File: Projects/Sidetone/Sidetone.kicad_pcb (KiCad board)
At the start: 2 copper layers, 100 x 100 mm, 48 parts, among them Q1 2N3904, Q2 2N3904, Q3 2N3904, U1 4N35, U2 LM324, U3 LM386

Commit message: 20240216
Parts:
- moved C3 77.4 mm to (191.0, 94.5)
- moved R19 42.2 mm to (214.1, 44.2)
- moved R24 39.6 mm to (211.8, 63.0)
- moved C2 34.4 mm to (90.9, 56.4)
- moved C1 30.9 mm to (93.0, 36.9)
- moved R20 30.1 mm to (203.2, 36.6)
- moved R23 25.0 mm to (197.6, 55.4)
- moved R22 23.9 mm to (186.7, 66.0)
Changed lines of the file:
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@@
   (net 35 "unconnected-(U3-GAIN-Pad1)")
   (footprint "Capacitor_THT:CP_Radial_D8.0mm_P3.80mm" (layer "F.Cu")
-    (at 123.885058 46.443284)
+    (at 90.932 56.388)
     (descr "CP, Radial series, Radial, pin pitch=3.80mm, , diameter=8mm, Electrolytic Capacitor")
     (tags "CP Radial series Radial pin pitch 3.80mm  diameter 8mm Electrolytic Capacitor")
@@
   )
   (footprint "Resistor_THT:R_Axial_DIN0207_L6.3mm_D2.5mm_P7.62mm_Horizontal" (layer "F.Cu")
-    (at 173.16036 46.293284)
+    (at 186.69 66.04)
     (descr "Resistor, Axial_DIN0207 series, Axial, Horizontal, pin pitch=7.62mm, 0.25W = 1/4W, length*diameter=6.3*2.5mm^2, http://cdn-reichelt.de/documents/datenblatt/B400/1_4W%23YAG.pdf")
     (tags "Resistor Axial_DIN0207 series Axial Horizontal pin pitch 7.62mm 0.25W = 1/4W length 6.3mm diameter 2.5mm")
@@
   )
   (footprint "Capacitor_THT:CP_Radial_D8.0mm_P3.80mm" (layer "F.Cu")
-    (at 123.885058 36.893284)
+    (at 92.964 36.893284)
     (descr "CP, Radial series, Radial, pin pitch=3.80mm, , diameter=8mm, Electrolytic Capacitor")
     (tags "CP Radial series Radial pin pitch 3.80mm  diameter 8mm Electrolytic Capacitor")
@@
   )
   (footprint "Resistor_THT:R_Axial_DIN0207_L6.3mm_D2.5mm_P7.62mm_Horizontal" (layer "F.Cu")
-    (at 173.16036 54.393284)
+    (at 211.836 62.992)
     (descr "Resistor, Axial_DIN0207 series, Axial, Horizontal, pin pitch=7.62mm, 0.25W = 1/4W, length*diameter=6.3*2.5mm^2, http://cdn-reichelt.de/documents/datenblatt/B400/1_4W%23YAG.pdf")
     (tags "Resistor Axial_DIN0207 series Axial Horizontal pin pitch 7.62mm 0.25W = 1/4W length 6.3mm diameter 2.5mm")
@@
   )
   (footprint "Resistor_THT:R_Axial_DIN0207_L6.3mm_D2.5mm_P7.62mm_Horizontal" (layer "F.Cu")
-    (at 173.16036 34.143284)
+    (at 214.122 44.196)
     (descr "Resistor, Axial_DIN0207 series, Axial, Horizontal, pin pitch=7.62mm, 0.25W = 1/4W, length*diameter=6.3*2.5mm^2, http://cdn-reichelt.de/documents/datenblatt/B400/1_4W%23YAG.pdf")
     (tags "Resistor Axial_DIN0207 series Axial Horizontal pin pitch 7.62mm 0.25W = 1/4W length 6.3mm diameter 2.5mm")
@@
   )
   (footprint "Resistor_THT:R_Axial_DIN0207_L6.3mm_D2.5mm_P7.62mm_Horizontal" (layer "F.Cu")
-    (at 173.16036 38.193284)
+    (at 203.2 36.576)
     (descr "Resistor, Axial_DIN0207 series, Axial, Horizontal, pin pitch=7.62mm, 0.25W = 1/4W, length*diameter=6.3*2.5mm^2, http://cdn-reichelt.de/documents/datenblatt/B400/1_4W%23YAG.pdf")
     (tags "Resistor Axial_DIN0207 series Axial Horizontal pin pitch 7.62mm 0.25W = 1/4W length 6.3mm diameter 2.5mm")
@@
   )
   (footprint "Resistor_THT:R_Axial_DIN0207_L6.3mm_D2.5mm_P7.62mm_Horizontal" (layer "F.Cu")
-    (at 173.16036 50.343284)
+    (at 197.612 55.372)
     (descr "Resistor, Axial_DIN0207 series, Axial, Horizontal, pin pitch=7.62mm, 0.25W = 1/4W, length*diameter=6.3*2.5mm^2, http://cdn-reichelt.de/documents/datenblatt/B400/1_4W%23YAG.pdf")
     (tags "Resistor Axial_DIN0207 series Axial Horizontal pin pitch 7.62mm 0.25W = 1/4W length 6.3mm diameter 2.5mm")
@@
   )
   (footprint "Capacitor_THT:CP_Radial_D8.0mm_P3.80mm" (layer "F.Cu")
-    (at 123.885058 55.993284)
+    (at 191.008 94.488)
     (descr "CP, Radial series, Radial, pin pitch=3.80mm, , diameter=8mm, Electrolytic Capacitor")
     (tags "CP Radial series Radial pin pitch 3.80mm  diameter 8mm Electrolytic Capacitor")

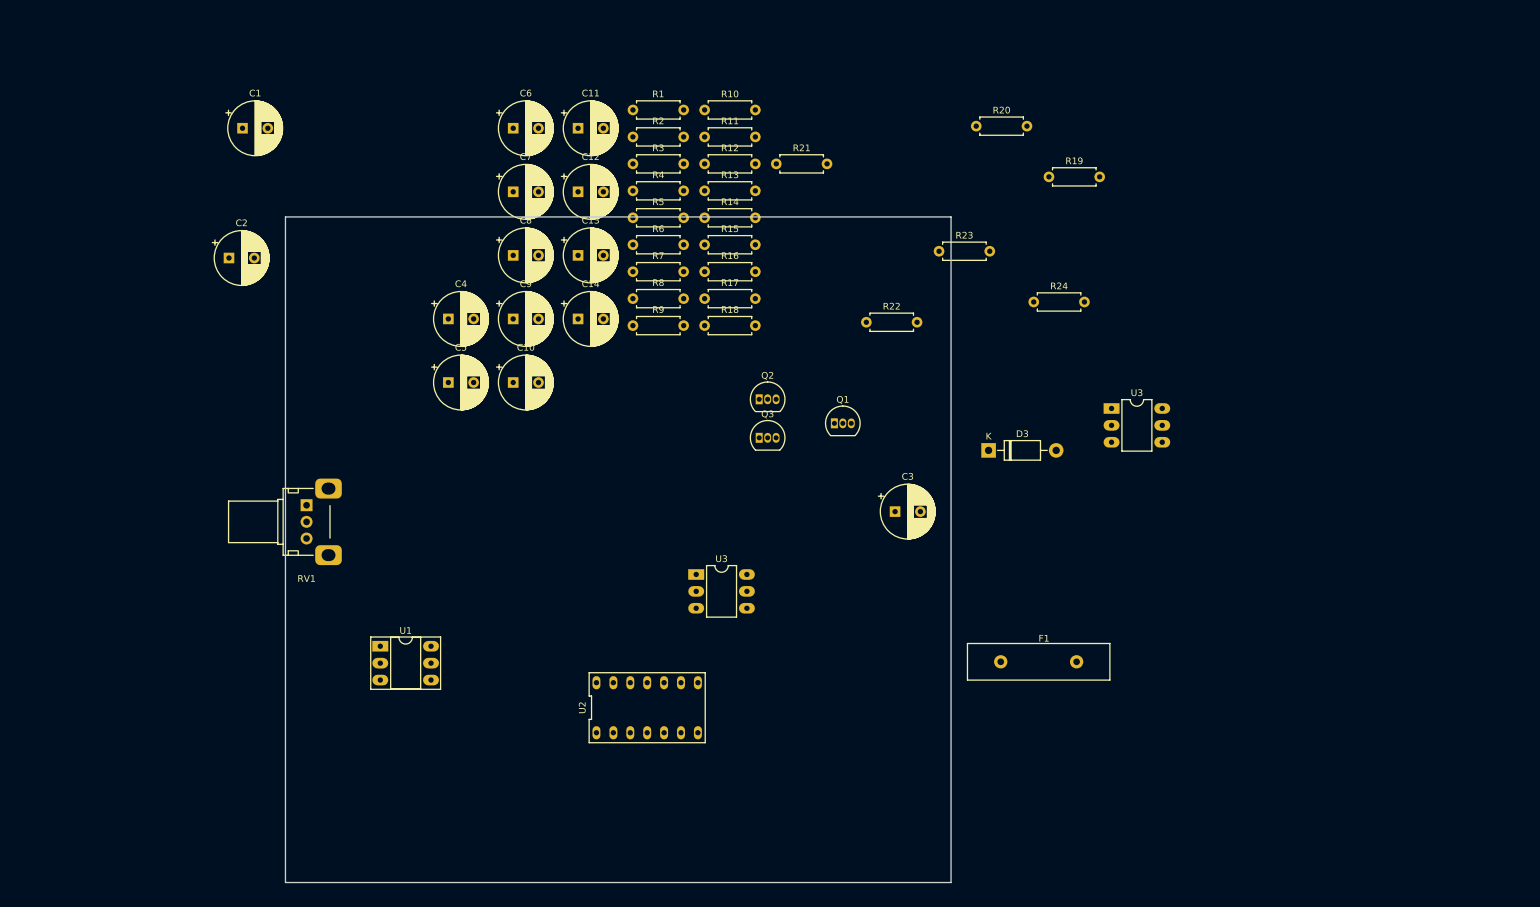
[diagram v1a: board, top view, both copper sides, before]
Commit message: modified sidetone schematic
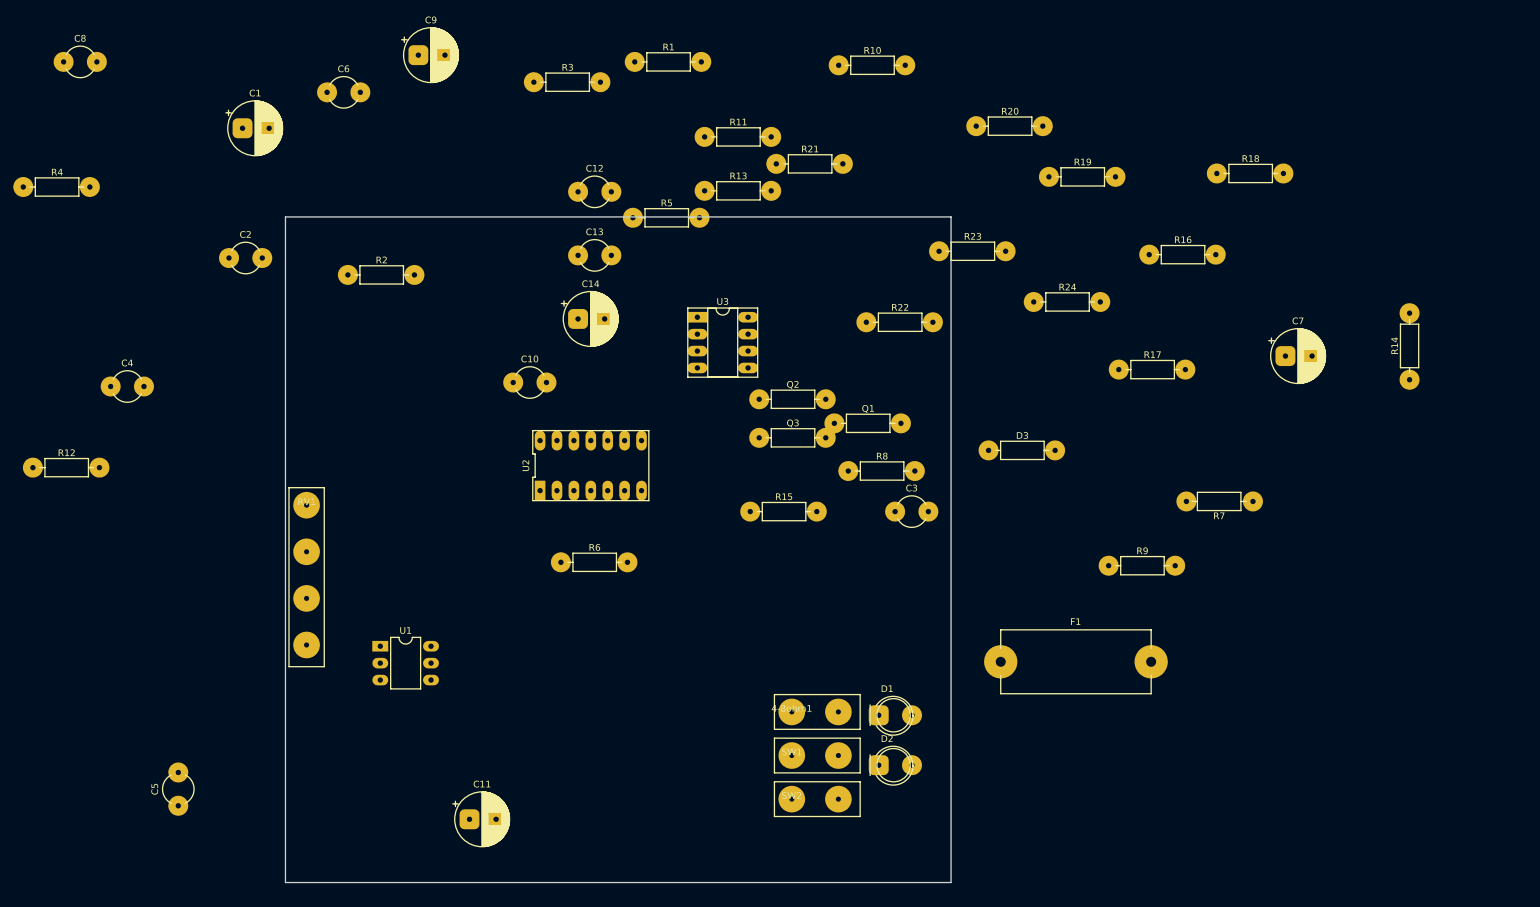
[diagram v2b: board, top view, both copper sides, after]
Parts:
- removed the U3 at (223.5, 79.0)
- added 4-8ohm1: Speaker, 000_Other_Device:Hangszoro, F.Cu at (175.5, 124.6)
- added D1: Red, 000_Diode:LED_D5.0mm_P5.0_Clear, F.Cu at (188.5, 125.1)
- added D2: Power (Green), 000_Diode:LED_D5.0mm_P5.0_Clear, F.Cu at (188.5, 132.6)
- added SW1: morse key, 000_Other_Device:Morse_Key_Pad_Group_2Pin_P7mm, F.Cu at (175.5, 131.1)
- added SW2: On/off, 000_Other_Device:Kapcsolo_Pad_Group_2Pin_P7mm, F.Cu at (175.5, 137.7)
- C1, C11, C14, C7, C9: footprint Capacitor_THT:CP_Radial_D8.0mm_P3.80mm -> 000_Capacitor:CP_Radial_Elektrolit_D8.0mm_P4.0mm_H12
- C10, C12, C13, C2, C3, C4, C5, C6, C8: footprint Capacitor_THT:CP_Radial_D8.0mm_P3.80mm -> 000_Capacitor:C_Radial_Ceramic_D4.5mm_P5.00mm
- D3: footprint Diode_THT:D_DO-41_SOD81_P10.16mm_Horizontal -> 000_Resistor:R_Axial_L6.3mm_D2.5mm_P10.0mm_Horizontal
- F1: footprint Fuse:Fuse_Littelfuse-LVR125 -> 000_Other_Device:Fuseholder_22x10mm_Horizontal
- Q1, Q2, Q3: footprint Package_TO_SOT_THT:TO-92_Inline -> 000_Resistor:R_Axial_L6.3mm_D2.5mm_P10.0mm_Horizontal
- R1, R10, R11, R12, R13, R14, R15, R16, R17, R18, R19, R2, R20, R21, R22, R23, R24, R3, R4, R5, R6, R7, R8, R9: footprint Resistor_THT:R_Axial_DIN0207_L6.3mm_D2.5mm_P7.62mm_Horizontal -> 000_Resistor:R_Axial_L6.3mm_D2.5mm_P10.0mm_Horizontal
- RV1: footprint Potentiometer_THT:Potentiometer_Alps_RK09K_Single_Horizontal -> 000_Resistor:Potenciometer_4Pin_P7mm
- U1: footprint Package_DIP:DIP-6_W7.62mm_Socket_LongPads -> 000_IC:DIP-6_W7.62mm_LongPads
- U2: footprint 001_user_library:DIP-14_296_ELL_LM324 -> 000_IC:DIP-14_LM324
- U3: footprint Package_DIP:DIP-6_W7.62mm_LongPads -> 000_IC:DIP-8_W7.62mm_Socket_LongPads
- moved C7 118.6 mm to (249.7, 71.1)
- moved R12 110.8 mm to (61.5, 87.9)
- moved R14 108.7 mm to (268.3, 74.7), turned to 90 degrees
- moved C11 105.1 mm to (127.1, 140.7)
- moved R7 99.3 mm to (244.8, 93.0), turned to 180 degrees
- moved R4 91.6 mm to (60.0, 45.7)
- moved R18 80.3 mm to (239.3, 43.7)
- moved R9 80.1 mm to (223.1, 102.6)
- moved C5 75.4 mm to (83.3, 138.7), turned to 90 degrees
- moved C8 73.5 mm to (66.1, 26.9)
- moved R16 66.8 mm to (229.2, 55.9)
- moved R17 63.1 mm to (224.6, 73.2)
- moved C4 51.7 mm to (73.2, 75.7)
- moved R6 48.9 mm to (140.8, 102.1)
- moved R2 47.6 mm to (108.8, 58.9)
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
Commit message: 18-2
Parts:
- Q1, Q2, Q3: footprint 000_Resistor:R_Axial_L6.3mm_D2.5mm_P10.0mm_Horizontal -> 000_Transistor:TO-92_Kis_Muanyag_Hazas_Transistor
- moved Q3 34.5 mm to (151.0, 111.8)
- moved R11 9.28 mm to (166.7, 30.0)
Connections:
- R15 pad 1: Net-(C7-Pad1) -> Net-(R15-Pad1)
- R17 pad 2: Net-(C7-Pad1) -> Net-(R15-Pad1)
- R8 pad 1: Net-(C7-Pad1) -> Net-(R15-Pad1)

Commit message: 2
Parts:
- moved R12 102.1 mm to (162.6, 101.6)
- moved 4-8ohm1 61.2 mm to (157.5, 66.1), turned to 90 degrees
- moved C12 60.1 mm to (195.5, 76.2), turned to 180 degrees
- moved Q1 42.8 mm to (156.2, 115.5), turned to 90 degrees
- moved Q2 37.9 mm to (170.2, 115.5), turned to 90 degrees
- moved C3 35.9 mm to (158.5, 79.3), turned to -90 degrees
- moved C10 33.9 mm to (166.4, 83.8), turned to 90 degrees
- moved R6 26.3 mm to (123.2, 82.6), turned to -90 degrees
- moved RV1 25.6 mm to (104.1, 67.9)
- moved Q3 23.5 mm to (166.4, 129.5), turned to 180 degrees
- moved U1 23.5 mm to (133.3, 127.5)
- moved U3 12.0 mm to (170.2, 57.1)
- moved U2 9.57 mm to (138.2, 94.0), turned to -90 degrees

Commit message: 20240220
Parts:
- moved R7 132.1 mm to (113.0, 84.0), turned to -90 degrees
- moved R19 128.3 mm to (121.9, 133.3), turned to 90 degrees
- moved R1 117.8 mm to (110.5, 137.2), turned to -90 degrees
- moved R11 111.9 mm to (152.5, 141.0)
- moved R14 111.2 mm to (157.5, 83.9), turned to -90 degrees
- moved R17 109.0 mm to (144.7, 147.3), turned to 180 degrees
- moved R18 102.3 mm to (176.5, 124.4), turned to 90 degrees
- moved C6 102.1 mm to (129.5, 130.8), turned to 90 degrees
- moved R20 97.9 mm to (160.1, 124.5)
- moved C8 94.6 mm to (125.7, 100.3), turned to 180 degrees
- moved R9 91.1 mm to (133.4, 86.4)
- moved R5 90.7 mm to (135.9, 139.7), turned to 90 degrees
- moved R13 86.9 mm to (142.2, 130.8), turned to -90 degrees
- moved R16 86.6 mm to (160.0, 108.0), turned to 180 degrees
- moved R3 85.2 mm to (171.4, 107.8), turned to 90 degrees
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
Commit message: 20240222
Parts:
- removed the R4 at (116.9, 106.7)
- added +12Vf1: ~, 000_Other_Device:+12Vf, F.Cu at (91.7, 89.1)
- added GND1: ~, 000_Other_Device:GND, F.Cu at (151.3, 123.5)
- added R5: 220 K, 000_Resistor:R_Axial_L6.3mm_D2.5mm_P10.0mm_Horizontal, F.Cu at (132.0, 86.5)
- added Vcc1: ~, 000_Other_Device:+Vcc, F.Cu at (103.0, 122.4)
- moved C13 143.6 mm to (257.8, 72.5)
- moved R23 130.6 mm to (274.4, 114.4), turned to 0 degrees
- moved R22 109.2 mm to (284.4, 110.6), turned to 180 degrees
- moved C6 108.1 mm to (236.1, 113.1), turned to 180 degrees
- moved Q2 96.5 mm to (247.7, 133.4)
- moved R10 96.5 mm to (256.5, 80.1)
- moved R11 96.5 mm to (249.0, 142.3)
- moved R15 96.5 mm to (232.5, 124.5)
- moved R17 96.5 mm to (241.2, 148.7)
- moved R4 96.5 mm to (232.4, 141.1)
- moved R8 96.5 mm to (260.4, 95.2)
- moved C14 96.5 mm to (222.1, 77.5)
- moved D1 96.5 mm to (213.4, 146.1)
- moved R1 96.5 mm to (207.0, 138.6)
- moved R19 96.5 mm to (218.4, 134.7)
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- renumbered R5 to R4
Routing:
- net VCC: track 0.00 -> 122.3 mm
- net Net-(C3-Pad1): track 0.00 -> 46.0 mm
- net Net-(Q3-C): track 0.00 -> 44.1 mm
- net GNDD: track 0.00 -> 42.8 mm
- net Net-(U2C-+): track 0.00 -> 40.5 mm
- net Net-(R6-Pad1): track 0.00 -> 36.2 mm
- net Net-(C4-Pad2): track 0.00 -> 27.5 mm
- net Net-(U2A--): track 0.00 -> 22.3 mm
- net Net-(U2D--): track 0.00 -> 22.1 mm
- net Net-(SW2A-A): track 0.00 -> 19.9 mm
- net Net-(U2A-+): track 0.00 -> 15.6 mm
- net Net-(U2C--): track 0.00 -> 13.1 mm
- net Net-(Q1-C): track 0.00 -> 9.75 mm
- net Net-(Q1-E): track 0.00 -> 7.48 mm
- net Net-(Q3-B): track 0.00 -> 7.04 mm
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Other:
- board size 100 x 100 mm -> 80.6 x 80 mm
- board text added: "+"
- board text added: "+12V"
- board text added: "GND"
- board text added: "K"

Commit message: building pcb 20240222
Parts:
- removed +12Vf1: ~, 000_Other_Device:+12Vf
- moved R8 158.0 mm to (106.6, 131.5)
- moved R22 141.0 mm to (144.6, 92.5), turned to -90 degrees
- moved C10 139.2 mm to (127.6, 88.0), turned to -90 degrees
- moved R10 137.3 mm to (120.4, 97.5), turned to 90 degrees
- moved C6 128.8 mm to (111.7, 79.6), turned to -90 degrees
- moved Q1 126.5 mm to (136.6, 100.5)
- moved R19 125.0 mm to (107.2, 77.6), turned to -90 degrees
- moved Q3 124.5 mm to (127.1, 103.5), turned to 180 degrees
- moved R23 124.4 mm to (150.6, 102.5), turned to 90 degrees
- moved C12 114.6 mm to (161.1, 107.5)
- moved Q2 112.9 mm to (137.6, 108.5), turned to 180 degrees
- moved R12 111.0 mm to (147.5, 106.9), turned to 90 degrees
- moved D2 109.6 mm to (175.6, 82.0), turned to 90 degrees
- moved C8 108.2 mm to (113.6, 91.8), turned to -90 degrees
- moved R4 105.8 mm to (128.6, 120.5), turned to 0 degrees
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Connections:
- C11 pad 1: VCC -> Net-(D3-K)
- C6 pad 2: Net-(C6-Pad2) -> Net-(U2E-V+)
- C8 pad 1: Net-(C6-Pad2) -> Net-(U2E-V+)
- C9 pad 1: VCC -> Net-(U2E-V+)
- D3 pad 1: VCC -> Net-(D3-K)
- F1 pad 1: VCC -> Net-(D3-K)
- R1 pad 1: VCC -> Net-(D1-A)
- R1 pad 2: Net-(D1-A) -> Net-(D3-K)
- R11 pad 1: VCC -> Net-(U2E-V+)
- R13 pad 1: VCC -> Net-(U2E-V+)
- R19 pad 2: Net-(C6-Pad2) -> Net-(U2E-V+)
- R2 pad 1: VCC -> Net-(U2E-V+)
- R20 pad 1: VCC -> Net-(U2E-V+)
- R21 pad 1: VCC -> Net-(U2E-V+)
- R21 pad 2: VCC -> Net-(D3-K)
- R24 pad 1: VCC -> Net-(D3-K)
- U1 pad 5: VCC -> Net-(U2E-V+)
- U2 pad 4: VCC -> Net-(U2E-V+)
- U2 pad 7: Net-(C6-Pad2) -> Net-(U2E-V+)
- U3 pad 6: VCC -> Net-(D3-K)
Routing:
- net Net-(D3-K): track 0.00 -> 161.0 mm
- net Net-(U2E-V+): track 0.00 -> 101.6 mm
- net VCC: track 122.3 -> 25.0 mm
- net Net-(Q1-C): track 9.75 -> 43.1 mm
- net Net-(R6-Pad1): track 36.2 -> 5.57 mm
- net Net-(C3-Pad1): track 46.0 -> 25.0 mm
- net Net-(Q3-C): track 44.1 -> 61.6 mm
- net Net-(U2A--): track 22.3 -> 38.4 mm
- net GNDD: track 42.8 -> 55.2 mm
- net Net-(U2C-+): track 40.5 -> 30.2 mm, vias 0 -> 2
- net Net-(U2C--): track 13.1 -> 22.0 mm
- net Net-(Q1-E): track 7.48 -> 0.00 mm
- net Net-(Q3-B): track 7.04 -> 0.00 mm
- net Net-(SW2A-A): track 19.9 -> 13.2 mm
- net Net-(C6-Pad2): track 4.31 -> 0.00 mm
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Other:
- board size 80.6 x 80 mm -> 90.6 x 92 mm
- board text added: "+12V táp"
- board text added: "ák-1"
- board text removed: "+"
- board text removed: "+12V"

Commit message: 20240223
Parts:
- moved R15 54.1 mm to (101.9, 124.3)
- moved R5 37.3 mm to (137.2, 123.4), turned to 180 degrees
- moved C7 7.60 mm to (175.8, 56.0), turned to 180 degrees
- moved 4-8ohm1 5.61 mm to (136.0, 133.0), turned to 0 degrees
- moved C14 4.30 mm to (165.1, 113.3), turned to -90 degrees
- moved SW1 4.15 mm to (121.3, 134.4)
- moved D1 3.99 mm to (114.6, 115.7)
- moved GND1 3.59 mm to (152.0, 130.0)
- moved R21 3.30 mm to (182.0, 73.0)
- moved R8 3.14 mm to (109.0, 129.5)
- moved RV1 2.58 mm to (105.0, 94.7)
- moved C8 2.12 mm to (113.1, 89.7)
- moved R11 1.91 mm to (175.0, 117.2)
- moved R1 1.51 mm to (114.0, 126.0), turned to -90 degrees
- moved R4 1.14 mm to (127.5, 120.9)
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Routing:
- net GNDD: track 55.2 -> 644.8 mm, vias 0 -> 6
- net Net-(Q3-C): track 61.6 -> 210.5 mm, vias 0 -> 2
- net Net-(Q1-B): track 0.00 -> 44.8 mm, vias 0 -> 2
- net Net-(D3-K): track 161.0 -> 204.4 mm
- net Net-(C7-Pad1): track 0.00 -> 41.4 mm
- net Net-(Q3-B): track 0.00 -> 26.8 mm, vias 0 -> 2
- net Net-(SW1A-A): track 0.00 -> 24.8 mm
- net Net-(C13-Pad1): track 0.00 -> 18.9 mm
- net Net-(C12-Pad1): track 0.00 -> 18.6 mm
- net Net-(U2E-V+): track 101.6 -> 119.8 mm
- net Net-(Q2-B): track 0.00 -> 17.9 mm
- net Net-(Q1-E): track 0.00 -> 15.7 mm
- net Net-(Q2-E): track 0.00 -> 10.6 mm
- net Net-(D2-A): track 0.00 -> 9.53 mm
- net Net-(R15-Pad1): track 0.00 -> 9.20 mm
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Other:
- board size 90.6 x 92 mm -> 101.6 x 102 mm
- board text added: "ák1"
- board text added: "ák2"
- board text added: "ák3"
- board text added: "ák4"
- board text added: "ák5"
- board text added: "ák6"
- board text removed: "ák-1"
